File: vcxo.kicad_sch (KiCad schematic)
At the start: 30 parts

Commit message: Schematic updated
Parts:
- removed C?: 4.7u, symbol Device:C
- added C603: 22u, symbol Device:C_Polarized
- added C604: 100n, Capacitor_SMD:C_0805_2012Metric, symbol Device:C
- added FB601: FerriteBead, symbol Device:FerriteBead
- C601, C606, C613, C614: renamed from C?; footprint (none) -> Capacitor_SMD:C_0805_2012Metric; Remarks (none) -> Class 1
- C602: renamed from C?; Remarks (none) -> >=10V, low leak
- C605, C607, C608, C609, C610, C611, C612: renamed from C?; footprint (none) -> Capacitor_SMD:C_0805_2012Metric
- R601, R602, R603, R604, R605: renamed from R?; footprint (none) -> Resistor_SMD:R_0805_2012Metric
- TP601: renamed from TP?; footprint (none) -> TestPoint:TestPoint_THTPad_D1.0mm_Drill0.5mm
- gave numbers to parts that had none: 7
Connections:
- net +3.3VA: now also C604.2, FB601.1; no longer C608.2, C609.2, C610.2, C611.2, C612.2, R603.2, U601.1 (VDD), U604.5, U605.5, X601.4 (VDD), X602.6 (VCC)
- net GND: now also C603.2, C604.1
- net at C607.1, R603.1, U602.1 (VDD)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: now also C603.1
- net at C613.1, R604.1, U604.1: no longer R605.1
- net at C614.2, R604.2: now also R605.1
- new net +3.3VD: C610.2, C611.2, C612.2, U601.1 (VDD), U604.5, U605.5
- new net +5VMAIN: R603.2
- new net VCXO_VCC: C608.2, C609.2, FB601.2, X601.4 (VDD), X602.6 (VCC)
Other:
- moved on the sheet: C601, C602, C606, C614, R601, R602, R605

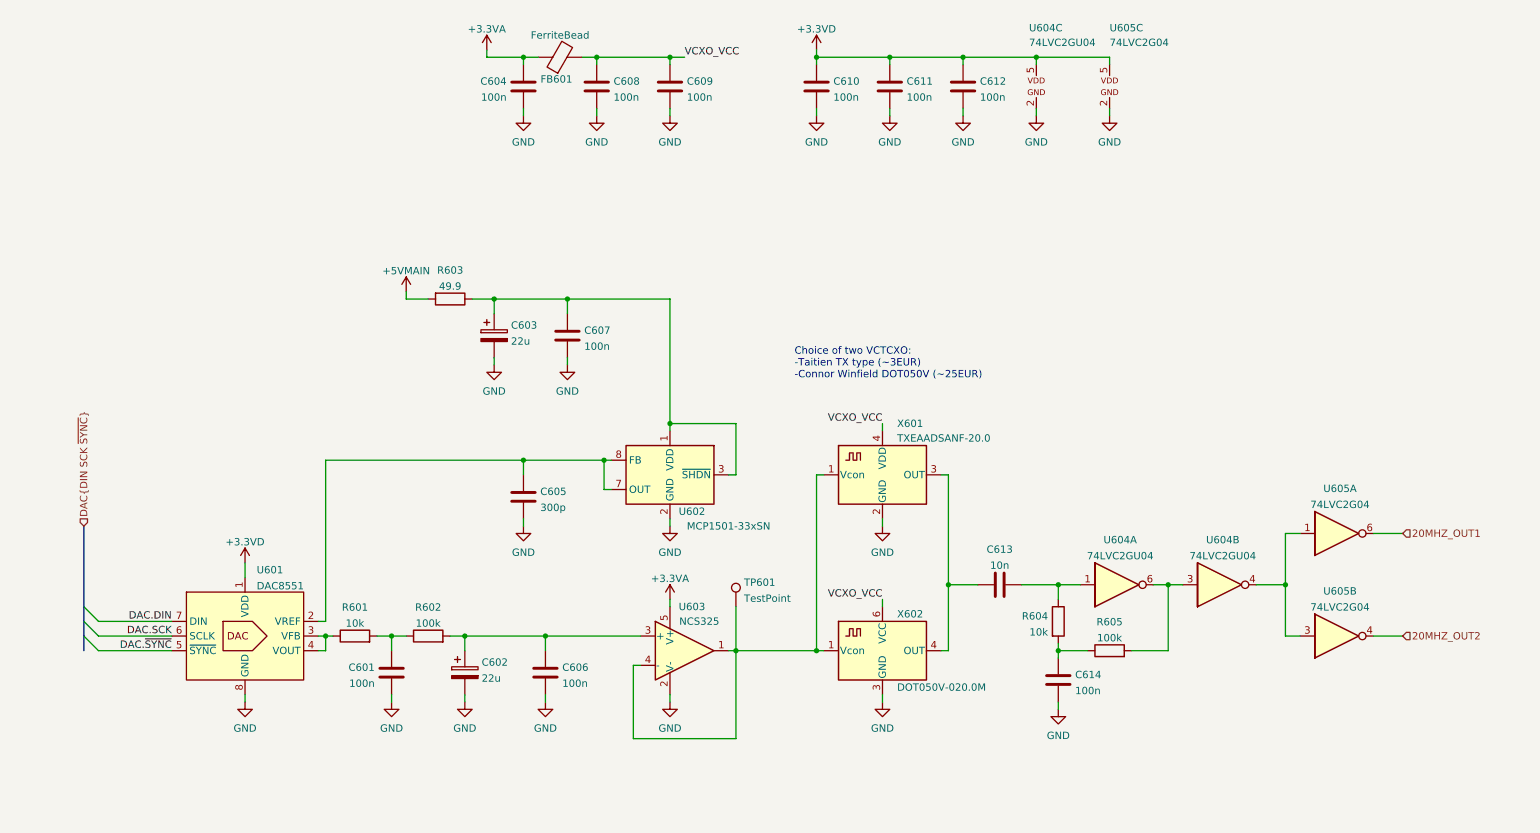
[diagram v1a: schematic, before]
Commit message: Schematic sketching done
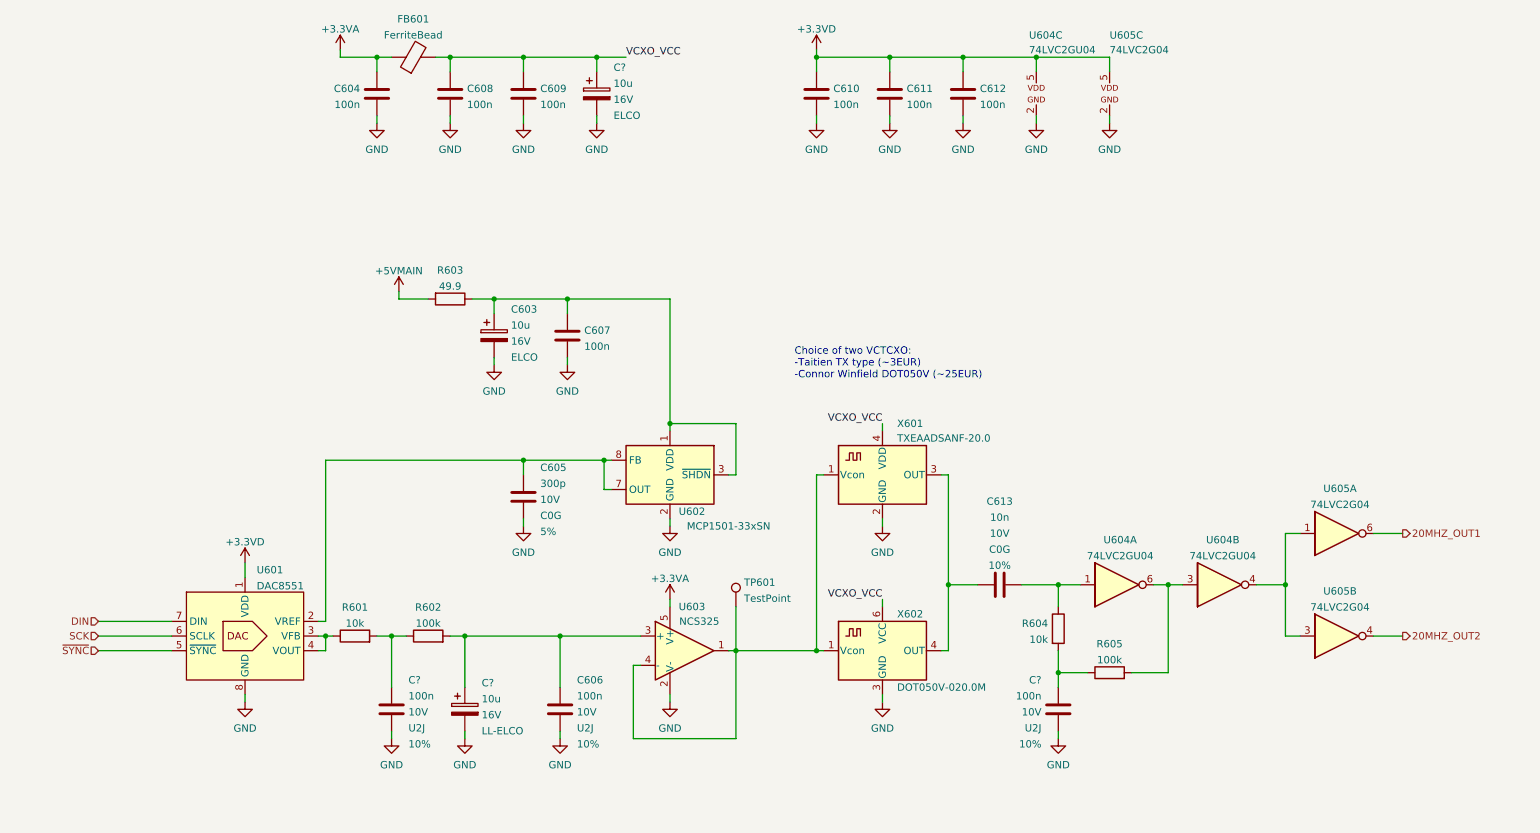
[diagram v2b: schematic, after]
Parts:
- removed C601, C614: 100n, Capacitor_SMD:C_0805_2012Metric, symbol Device:C
- removed C602: 22u, symbol Device:C_Polarized
- added C? (x2): 100n, Capacitor_SMD:C_0805_2012Metric, symbol Device:C
- added C? (x2): 10u, symbol Device:C_Polarized
- C603: value 22u -> 10u; Spec1 (none) -> 16V; Spec2 (none) -> ELCO
- C605: Spec1 (none) -> 10V; Spec2 (none) -> C0G; Tolerance (none) -> 5%
- C606: Remarks Class 1 -> (none); Spec1 (none) -> 10V; Spec2 (none) -> U2J; Tolerance (none) -> 10%
- C613: Spec1 (none) -> 10V; Spec2 (none) -> C0G; Tolerance (none) -> 10%
- R601, R602, R603, R604, R605: Tolerance (none) -> 5%
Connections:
- net GND: now also C?.2, C?.2, C?.2, C?.2
- net VCXO_VCC: now also C?.1
- net at R601.2, R602.1: now also C?.1
- net at C606.1, R602.2, U603.3 (+): now also C?.1
- net at R604.2, R605.1: now also C?.1
- net DAC.DIN renamed DIN
- net DAC.SCK renamed SCK
- net DAC.~{SYNC} renamed ~{SYNC}
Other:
- moved on the sheet: C604, C606, C608, C609, C610, C611, C612, FB601, R604, R605, U604C, U605C

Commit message: Update schematic layout, separate into sheets
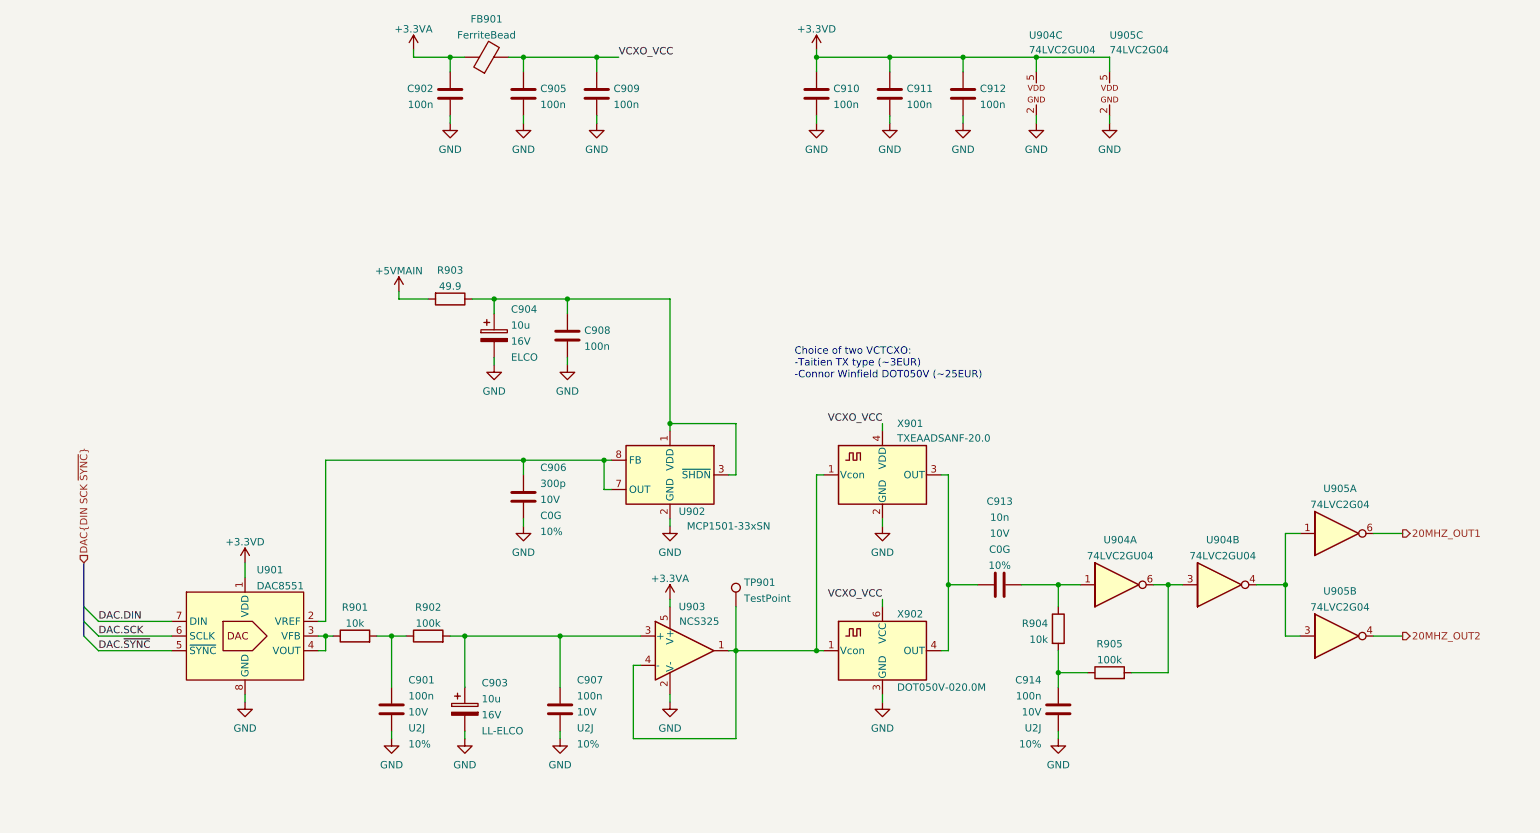
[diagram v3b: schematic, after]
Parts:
- removed C?: 10u, symbol Device:C_Polarized
- C906: renamed from C605; Tolerance 5% -> 10%
- gave numbers to parts that had none: 3
- renumbered C604 to C902, C603 to C904, C608 to C905, C606 to C907, C607 to C908, C609 to C909, C610 to C910, C611 to C911, C612 to C912, C613 to C913, FB601 to FB901, R601 to R901, R602 to R902, R603 to R903, R604 to R904, R605 to R905, TP601 to TP901, U601 to U901, U602 to U902, U603 to U903, U604 to U904, U605 to U905, X601 to X901, X602 to X902
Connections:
- net DIN renamed DAC.DIN
- net SCK renamed DAC.SCK
- net ~{SYNC} renamed DAC.~{SYNC}
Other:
- moved on the sheet: C902, C905, C909, FB901

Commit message: Schematic update
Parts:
- removed C903: 10u, symbol Device:C_Polarized
- removed C906: 300p, Capacitor_SMD:C_0805_2012Metric, symbol Device:C
- removed C907: 100n, Capacitor_SMD:C_0805_2012Metric, symbol Device:C
- added C903: 10n, Capacitor_SMD:C_0805_2012Metric, symbol Device:C
- added C905, C908: 1u, Capacitor_THT:C_Rect_L7.2mm_W5.5mm_P5.00mm_FKS2_FKP2_MKS2_MKP2, symbol Device:C
- added C910: 4.7u, Capacitor_SMD:C_0805_2012Metric, symbol Device:C
- added R904: 2.4k, Resistor_SMD:R_0805_2012Metric, symbol Device:R
- added R905: 100k, Resistor_SMD:R_0805_2012Metric, symbol Device:R
- added TP901: TestPoint, TestPoint:TestPoint_THTPad_D1.0mm_Drill0.5mm, symbol Connector:TestPoint
- C901: footprint Capacitor_SMD:C_0805_2012Metric -> Capacitor_SMD:C_1206_3216Metric; Spec1 10V -> 16V
- C902, C909: Spec1 (none) -> 16V; Spec2 (none) -> X5R; Tolerance (none) -> 20%
- C904: footprint (none) -> Capacitor_SMD:CP_Elec_4x5.8; Tolerance (none) -> 20%
- C906: renamed from C905; Spec1 (none) -> 16V; Spec2 (none) -> X5R; Tolerance (none) -> 20%
- C907: renamed from C908; Spec1 (none) -> 16V; Spec2 (none) -> X5R; Tolerance (none) -> 20%
- C911: renamed from C910; Spec1 (none) -> 16V; Spec2 (none) -> X5R; Tolerance (none) -> 20%
- C912: renamed from C911; Spec1 (none) -> 16V; Spec2 (none) -> X5R; Tolerance (none) -> 20%
- C913: renamed from C912; Spec1 (none) -> 16V; Spec2 (none) -> X5R; Tolerance (none) -> 20%
- C914: renamed from C913; Remarks Class 1 -> (none); Spec1 10V -> 16V
- C915: renamed from C914; footprint Capacitor_SMD:C_0805_2012Metric -> Capacitor_SMD:C_1206_3216Metric; Spec1 10V -> 16V
- renumbered R903 to R902, R902 to R903, R904 to R906, R905 to R907, TP901 to TP902
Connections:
- net GND: now also C903.2, C905.2, C908.2, C910.1, R904.1
- net VCXO_VCC: now also C910.2
- net at U901.2 (VREF), U902.7 (OUT), U902.8 (FB): now also C903.1, R904.2, TP901.1
- net at R903.2: now also C905.1, R905.1; no longer U903.3 (+)
- new net: C908.1, R905.2, U903.3 (+)
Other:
- note added: "High impedance path >> avoid any leakage <<"
- moved on the sheet: C901, C914, C915, R901, R903, R906, R907, TP902, U902, U903, U904A, U904B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

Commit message: Schematic: better LDO output capacitor selection, clarified BOM
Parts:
- removed C904: 10u, Capacitor_SMD:CP_Elec_4x5.8, symbol Device:C_Polarized
- removed C905, C908: 1u, Capacitor_THT:C_Rect_L7.2mm_W5.5mm_P5.00mm_FKS2_FKP2_MKS2_MKP2, symbol Device:C
- removed C907: 100n, Capacitor_SMD:C_0805_2012Metric, symbol Device:C
- removed C915: 100n, Capacitor_SMD:C_1206_3216Metric, symbol Device:C
- removed R903, R905: 100k, Resistor_SMD:R_0805_2012Metric, symbol Device:R
- added C906: 4.7u, Capacitor_SMD:C_0805_2012Metric, symbol Device:C
- added C912: 10n, Capacitor_SMD:C_0805_2012Metric, symbol Device:C
- C901: renamed from C902; Spec1 16V -> (none); Spec2 X5R -> (none); Tolerance 20% -> (none)
- C902: renamed from C903; Spec1 16V -> 25V
- C903: renamed from C906; Spec1 16V -> (none); Spec2 X5R -> (none); Tolerance 20% -> (none)
- C904: renamed from C901; Spec1 16V -> 25V
- C905: renamed from C909; Spec1 16V -> (none); Spec2 X5R -> (none); Tolerance 20% -> (none)
- C907: renamed from C910; Spec1 16V -> (none); Spec2 X5R -> (none); Tolerance 20% -> (none)
- C908: renamed from C911; Spec1 16V -> (none); Spec2 X5R -> (none); Tolerance 20% -> (none)
- C909: renamed from C912; Spec1 16V -> (none); Spec2 X5R -> (none); Tolerance 20% -> (none)
- C910: renamed from C913; value 100n -> 1u; Spec1 16V -> (none); Spec2 X5R -> (none); Tolerance 20% -> (none)
- C911: renamed from C914; value 10n -> 1n; Spec1 16V -> 25V
- FB901: value FerriteBead -> 782853701; footprint (none) -> Inductor_SMD:L_0805_2012Metric_Pad1.05x1.20mm_HandSolder
- renumbered R904 to R903, R906 to R904, R907 to R905
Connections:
- net GND: now also C906.1, C912.2
- net at C904.1, R901.2: now also U903.3 (+)
- net at R902.1, U902.1 (VDD), U902.3 (~{SHDN}): now also C906.2
- net at R904.2, R905.1: now also C912.1
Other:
- note removed: "High impedance path >> avoid any leakage <<"
- moved on the sheet: C902, C904, R901, R902, R903, TP901, U901

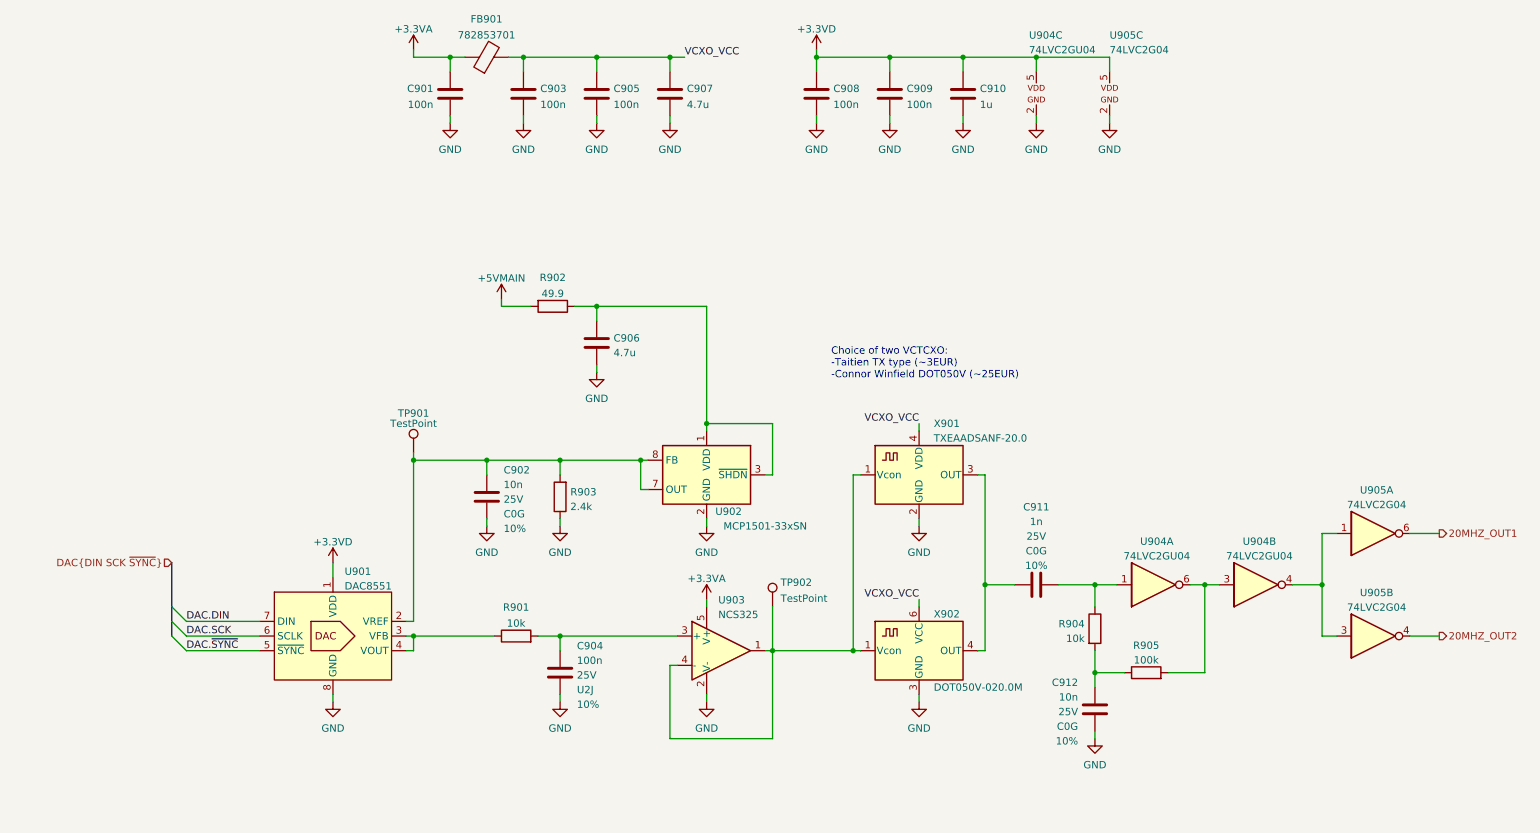
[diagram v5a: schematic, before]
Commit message: Schematic: yet another update -Improve way caps are specified once again -Update cap voltages based on ESD simulation -Make anti-aliasing LC filter more practical - with much less inductors -Specify Mfr & MfrPN for almost all components (most from Mouser, some from Digikey)
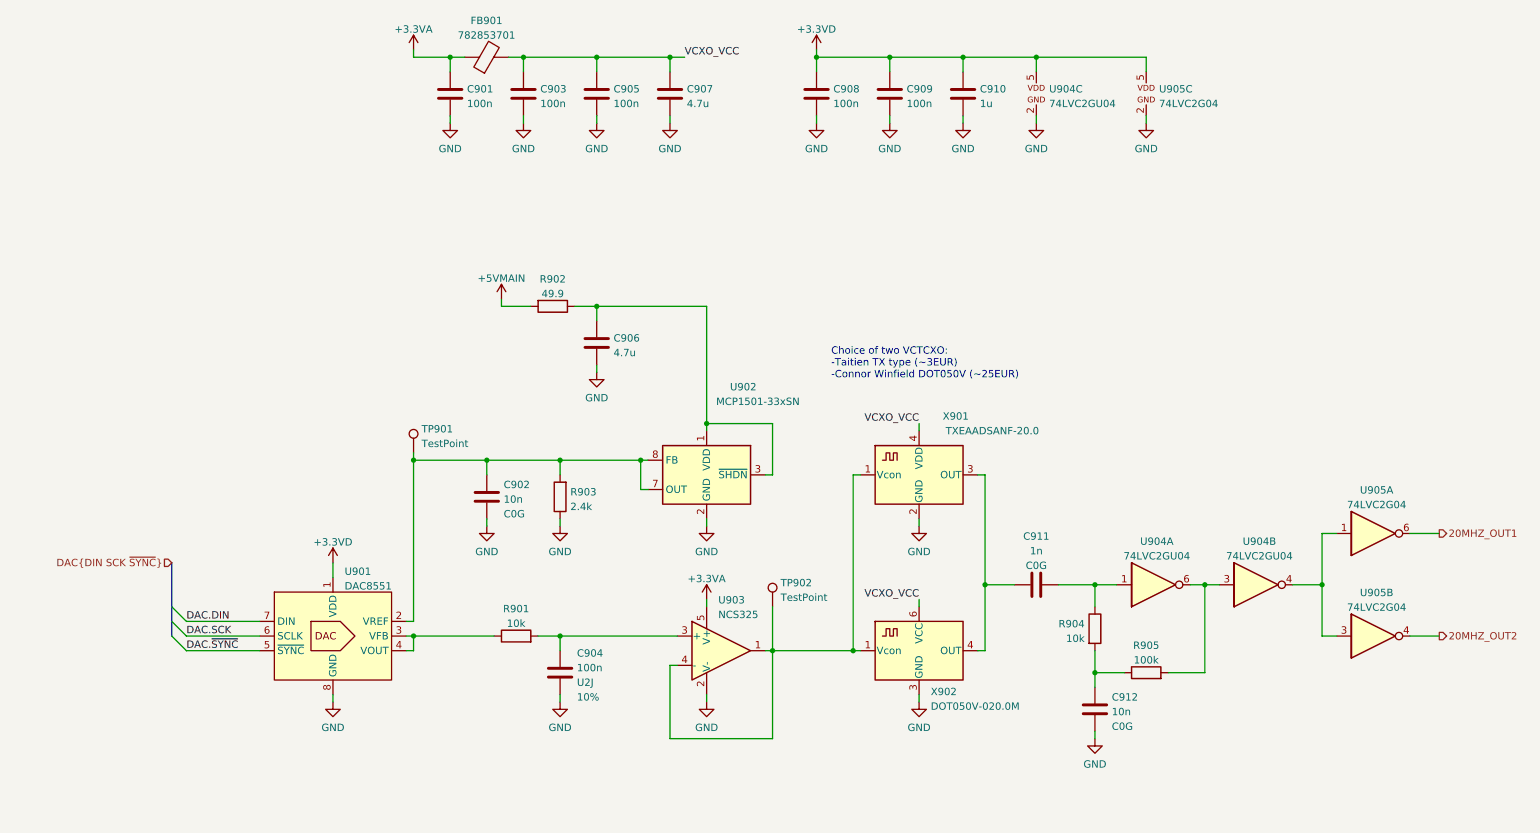
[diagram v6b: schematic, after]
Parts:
- C901, C903, C905, C908, C909: Mfr (none) -> Samsung; Mfr PN (none) -> CL21B104KBFNNNE
- C902, C912: Mfr (none) -> Murata; Mfr PN (none) -> GRM2165C2A103JA01; Spec1 25V -> (none); Tolerance 10% -> (none)
- C904: Mfr (none) -> KEMET; Mfr PN (none) -> C1206C104K5JACTU; Spec1 25V -> (none)
- C906, C907: Mfr (none) -> Murata; Mfr PN (none) -> GRM21BR71C475ME51
- C910: Mfr (none) -> Samsung; Mfr PN (none) -> CL21B105KOFNNNG
- C911: Mfr (none) -> KEMET; Mfr PN (none) -> C0805C102J5GAC; Spec1 25V -> (none); Tolerance 10% -> (none)
- FB901: Mfr (none) -> Wurth; Mfr PN (none) -> 782853701
- R901, R902, R903, R904, R905: Tolerance 5% -> (none)
- U901: Mfr (none) -> Texas Instruments; Mfr PN (none) -> DAC8551IADGKR
- U902: Mfr (none) -> Microchip; Mfr PN (none) -> MCP1501-33E/SN
- U903: Mfr (none) -> Onsemi; Mfr PN (none) -> NCS325SN2T1G
- U904: Mfr (none) -> Texas Instruments; Mfr PN (none) -> 74LVC2GU04DBVRG4
- U905: Mfr (none) -> Nexperia; Mfr PN (none) -> 74LVC2G04GV-Q100H
- X901: Mfr (none) -> Taitien; Mfr PN (none) -> TXEAADSANF-20.0
- X902: Mfr (none) -> Connor Winfield; Mfr PN (none) -> DOT050V-020.0M
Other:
- moved on the sheet: U905C
